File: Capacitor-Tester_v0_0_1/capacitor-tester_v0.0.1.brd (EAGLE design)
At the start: 100 x 80 mm, 6 parts, among them U1 AD5933, Y1 LFSPXO018034

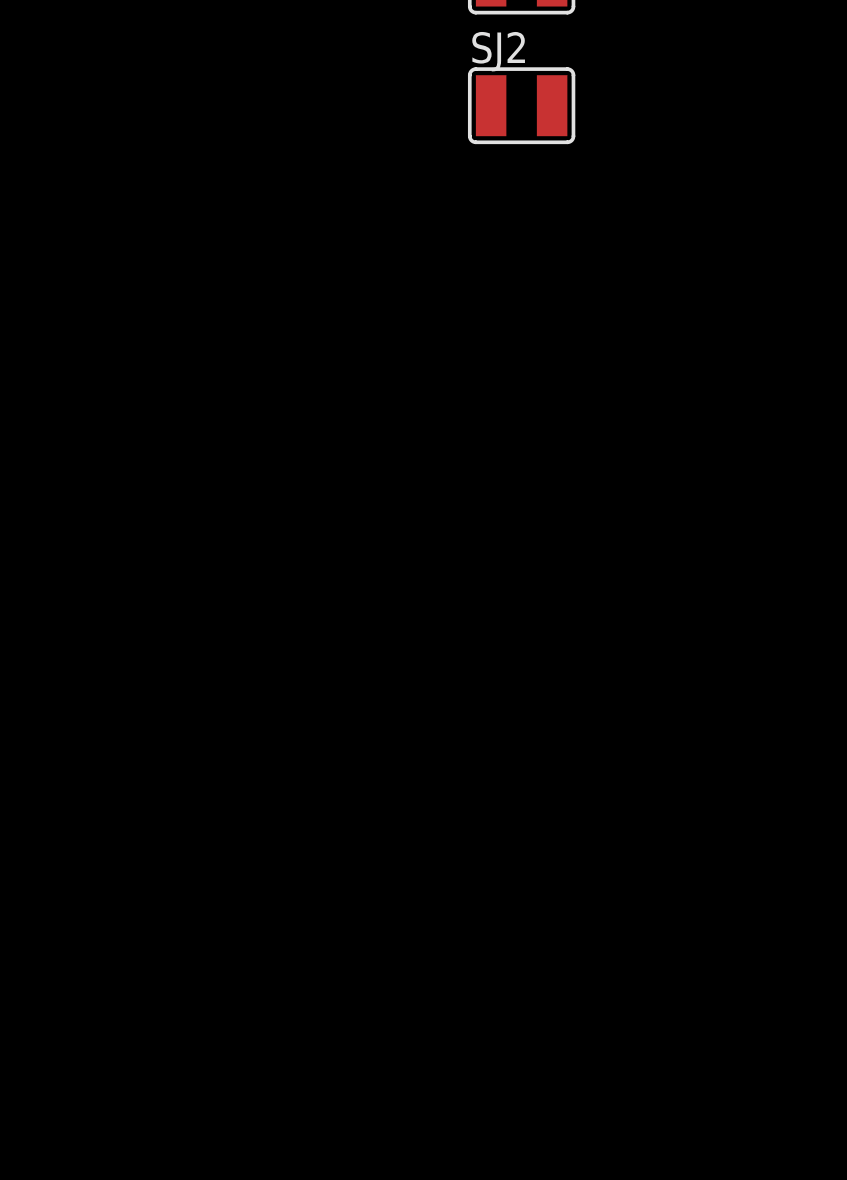
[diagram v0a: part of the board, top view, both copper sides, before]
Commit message: v0.0.1 - Finished the first stage of AD5933 opamp and added usb c connector for the power supply
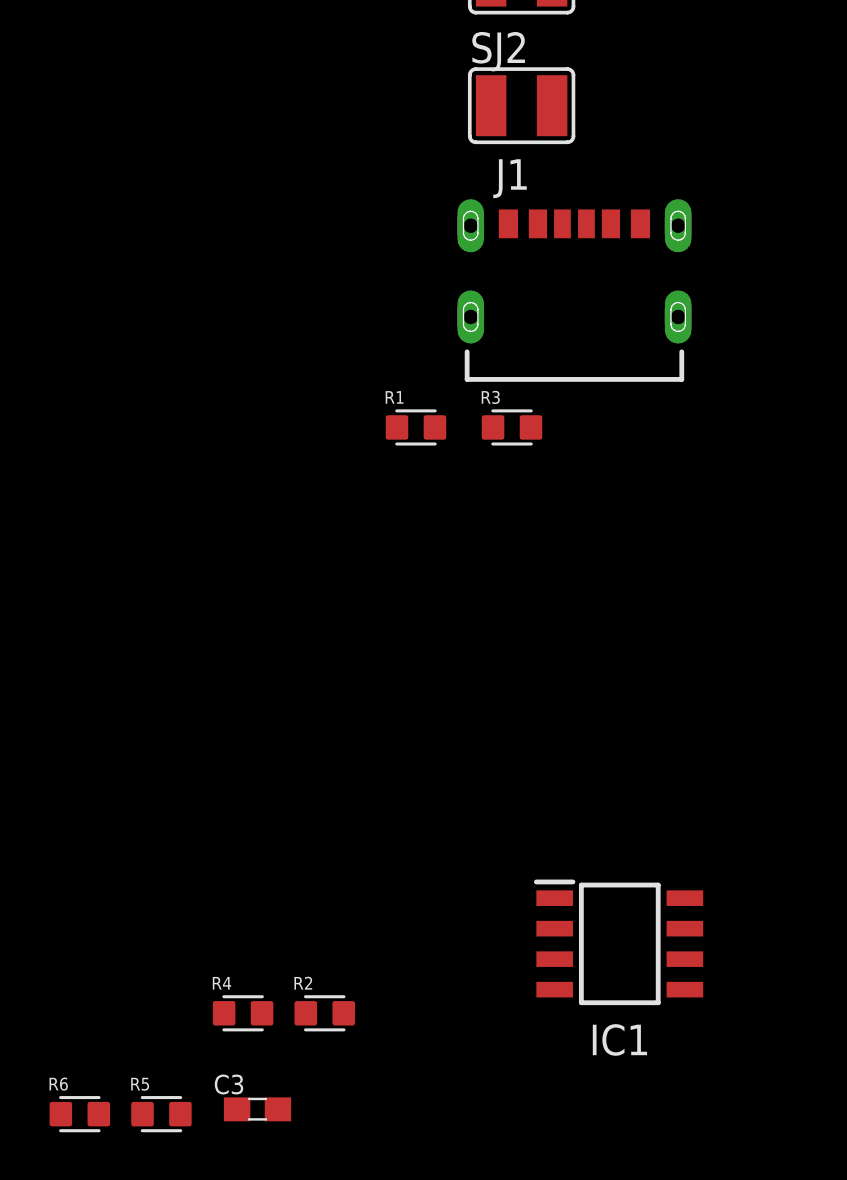
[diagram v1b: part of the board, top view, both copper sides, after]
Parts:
- added C3: 1u, custom_library:C0603
- added IC1: AD8531ARZ, AD8531ARZ:SOIC127P600X175-8N
- added J1: USB4125-GF-A-0190_REVA2, USB-C-6Pin:GCT_USB4125-GF-A-0190_REVA2
- added R1, R3: DNP4k7-1%, custom_library:R0603
- added R2, R5, R6: 20k-1%, custom_library:R0603
- added R4: 4k-1%, custom_library:R0603
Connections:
- new net N$1: IC1.2, R2.1, R4.1
- new net N$4: C3.1, IC1.3, R5.2, R6.1
- new net OPAMP_OUT: IC1.6, R4.2
- new net RFB: U1.4
- new net VIN: U1.5
- new net VOUT: R2.2, U1.6
- net +5V: now also IC1.7, J1.A9, J1.B9, R1.2, R3.2, R5.1
- net GND: now also C3.2, IC1.4, J1.A12, J1.B12, J1.S1, J1.S2, J1.S3, J1.S4, R6.2
- net SCL: now also R1.1
- net SDA: now also R3.1
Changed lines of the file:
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@@
 <attribute name="VALUE" x="-5.8" y="-73.4" size="0.02" layer="27"/>
+</element>
+<element name="J1" library="USB-C-6Pin" package="GCT_USB4125-GF-A-0190_REVA2" value="USB4125-GF-A-0190_REVA2" x="-4.6" y="-81.4" smashed="yes">
+<attribute name="AVAILABILITY" value="In Stock" x="-4.6" y="-81.4" size="1.778" layer="27" display="off"/>
+<attribute name="CHECK_PRICES" value="https://www.snapeda.com/parts/USB4125-GF-A-0190/Global+Connector+Technology/view-part/?ref=eda" x="-4.6" y="-81.4" size="1.778" layer="27" display="off"/>
+<attribute name="DESCRIPTION" value="                                                      USB-C (USB TYPE-C) USB 2.0 Receptacle Connector 24 (6+18 Dummy) Position Surface Mount, Right Angle; Through Hole                                              " x="-4.6" y="-81.4" size="1.778" layer="27" display="off"/>
+<attribute name="MF" value="Global Connector Technology" x="-4.6" y="-81.4" size="1.778" layer="27" display="off"/>
+<attribute name="MP" value="USB4125-GF-A-0190" x="-4.6" y="-81.4" size="1.778" layer="27" display="off"/>
+<attribute name="NAME" x="-7.9" y="-76.9" size="1.27" layer="25"/>
+<attribute name="PACKAGE" value="None" x="-4.6" y="-81.4" size="1.778" layer="27" display="off"/>
+<attribute name="PRICE" value="None" x="-4.6" y="-81.4" size="1.778" layer="27" display="off"/>
+<attribute name="SNAPEDA_LINK" value="https://www.snapeda.com/parts/USB4125-GF-A-0190/Global+Connector+Technology/view-part/?ref=snap" x="-4.6" y="-81.4" size="1.778" layer="27" display="off"/>
+</element>
+<element name="R3" library="custom_library" package="R0603" value="DNP4k7-1%" x="-7.2" y="-86.8" smashed="yes">
+<attribute name="NAME" x="-8.52476875" y="-85.813721875" size="0.52744375" layer="25"/>
+<attribute name="VALUE" x="-8.919259375" y="-88.32958125" size="0.525771875" layer="27"/>
+</element>
+<element name="R1" library="custom_library" package="R0603" value="DNP4k7-1%" x="-11.2" y="-86.8" smashed="yes">
+<attribute name="NAME" x="-12.52476875" y="-85.813721875" size="0.52744375" layer="25"/>
+<attribute name="VALUE" x="-12.919259375" y="-88.32958125" size="0.525771875" layer="27"/>
+</element>
+<element name="IC1" library="AD8531ARZ" package="SOIC127P600X175-8N" value="AD8531ARZ" x="-2.712" y="-108.31" smashed="yes">
+<attribute name="DESCRIPTION" value="250 mA Output, Low Cost, Single-Supply Amplifier" x="-2.712" y="-108.31" size="1.778" layer="27" display="off"/>
+<attribute name="HEIGHT" value="1.75mm" x="-2.712" y="-108.31" size="1.778" layer="27" display="off"/>
+<attribute name="MANUFACTURER_NAME" value="Analog Devices" x="-2.712" y="-108.31" size="1.778" layer="27" display="off"/>
+<attribute name="MANUFACTURER_PART_NUMBER" value="AD8531ARZ" x="-2.712" y="-108.31" size="1.778" layer="27" display="off"/>
+<attribute name="MOUSER_PART_NUMBER" value="584-AD8531ARZ" x="-2.712" y="-108.31" size="1.778" layer="27" display="off"/>
+<attribute name="MOUSER_PRICE-STOCK" value="https://www.mouser.co.uk/ProductDetail/Analog-Devices/AD8531ARZ?qs=%2FtpEQrCGXCxqCqynf0JWOw%3D%3D" x="-2.712" y="-108.31" size="1.778" layer="27" display="off"/>
+<attribute name="NAME" x="-2.712" y="-112.31" size="1.27" layer="25" align="center"/>
+<attribute name="VALUE" x="-2.712" y="-108.31" size="1.27" layer="27" align="center"/>
+</element>
+<element name="R2" library="custom_library" package="R0603" value="20k-1%" x="-15" y="-111.2" smashed="yes">
+<attribute name="NAME" x="-16.32476875" y="-110.213721875" size="0.52744375" layer="25"/>
+<attribute name="VALUE" x="-16.719259375" y="-112.72958125" size="0.525771875" layer="27"/>
+</element>
+<element name="R4" library="custom_library" package="R0603" value="4k-1%" x="-18.4" y="-111.2" smashed="yes">
+<attribute name="NAME" x="-19.72476875" y="-110.213721875" size="0.52744375" layer="25"/>
+<attribute name="VALUE" x="-20.119259375" y="-112.72958125" size="0.525771875" layer="27"/>
+</element>
+<element name="C3" library="custom_library" package="C0603" value="1u" x="-17.8" y="-115.2" smashed="yes">
+<attribute name="NAME" x="-19.635" y="-114.565" size="0.8" layer="25"/>
+<attribute name="VALUE" x="-18.435" y="-117.105" size="1.27" layer="27"/>
+</element>
+<element name="R5" library="custom_library" package="R0603" value="20k-1%" x="-21.8" y="-115.4" smashed="yes">
+<attribute name="NAME" x="-23.12476875" y="-114.413721875" size="0.52744375" layer="25"/>
+<attribute name="VALUE" x="-23.519259375" y="-116.92958125" size="0.525771875" layer="27"/>
+</element>
+<element name="R6" library="custom_library" package="R0603" value="20k-1%" x="-25.2" y="-115.4" smashed="yes">
+<attribute name="NAME" x="-26.52476875" y="-114.413721875" size="0.52744375" layer="25"/>
+<attribute name="VALUE" x="-26.919259375" y="-116.92958125" size="0.525771875" layer="27"/>
 </element>
 </elements>
@@
 <contactref element="C2" pad="2"/>
 <contactref element="Y1" pad="2"/>
+<contactref element="J1" pad="B12"/>
+<contactref element="J1" pad="A12"/>
+<contactref element="J1" pad="S1"/>
+<contactref element="J1" pad="S4"/>
+<contactref element="J1" pad="S2"/>
+<contactref element="J1" pad="S3"/>
+<contactref element="IC1" pad="4"/>
+<contactref element="C3" pad="2"/>
+<contactref element="R6" pad="2"/>
+<wire x1="-16.95" y1="-115.2" x2="-24.41" y2="-115.4" width="0" layer="19" extent="1-1"/>
+<wire x1="-5.424" y1="-110.215" x2="-16.95" y2="-115.2" width="0" layer="19" extent="1-1"/>
+<wire x1="-8.92" y1="-82.2" x2="-5.424" y2="-110.215" width="0" layer="19" extent="1-1"/>
+<wire x1="-8.92" y1="-78.4" x2="-8.92" y2="-82.2" width="0" layer="19" extent="1-1"/>
+<wire x1="-7.35" y1="-78.32" x2="-8.92" y2="-78.4" width="0" layer="19" extent="1-1"/>
+<wire x1="-1.85" y1="-78.32" x2="-7.35" y2="-78.32" width="0" layer="19" extent="1-1"/>
+<wire x1="-0.28" y1="-78.4" x2="-1.85" y2="-78.32" width="0" layer="19" extent="1-1"/>
+<wire x1="-0.28" y1="-82.2" x2="-0.28" y2="-78.4" width="0" layer="19" extent="1-1"/>
+<wire x1="0" y1="-59.8" x2="-0.28" y2="-78.4" width="0" layer="19" extent="1-1"/>
 <wire x1="-5.75" y1="-26.6" x2="0" y2="-59.8" width="0" layer="19" extent="1-1"/>
 <wire x1="-5.75" y1="-22.4" x2="-5.75" y2="-26.6" width="0" layer="19" extent="1-1"/>
@@
 <contactref element="Y1" pad="4"/>
 <contactref element="Y1" pad="1"/>
+<contactref element="J1" pad="B9"/>
+<contactref element="J1" pad="A9"/>
+<contactref element="R3" pad="2"/>
+<contactref element="R1" pad="2"/>
+<contactref element="IC1" pad="7"/>
+<contactref element="R5" pad="1"/>
+<wire x1="0" y1="-107.675" x2="-22.59" y2="-115.4" width="0" layer="19" extent="1-1"/>
+<wire x1="-6.41" y1="-86.8" x2="0" y2="-107.675" width="0" layer="19" extent="1-1"/>
+<wire x1="-10.41" y1="-86.8" x2="-6.41" y2="-86.8" width="0" layer="19" extent="1-1"/>
+<wire x1="-6.12" y1="-78.32" x2="-6.41" y2="-86.8" width="0" layer="19" extent="1-1"/>
+<wire x1="-3.08" y1="-78.32" x2="-6.12" y2="-78.32" width="0" layer="19" extent="1-1"/>
+<wire x1="-5.08" y1="-59.8" x2="-6.12" y2="-78.32" width="0" layer="19" extent="1-1"/>
 <wire x1="-5.08" y1="-55.6" x2="-5.08" y2="-59.8" width="0" layer="19" extent="1-1"/>
 <wire x1="-7.45" y1="-26.6" x2="-5.08" y2="-55.6" width="0" layer="19" extent="1-1"/>
@@
 <signal name="SCL">
 <contactref element="U1" pad="16"/>
+<contactref element="R1" pad="1"/>
+<wire x1="0" y1="-12.7" x2="-11.99" y2="-86.8" width="0" layer="19" extent="1-1"/>
 </signal>
 <signal name="SDA">
 <contactref element="U1" pad="15"/>
+<contactref element="R3" pad="1"/>
+<wire x1="0" y1="-13.35" x2="-7.99" y2="-86.8" width="0" layer="19" extent="1-1"/>
 </signal>
 <signal name="MCLK">
@@
 <contactref element="SJ2" pad="1"/>
 </signal>
+<signal name="RFB">
+<contactref element="U1" pad="4"/>
+</signal>
+<signal name="VIN">
+<contactref element="U1" pad="5"/>
+</signal>
+<signal name="VOUT">
+<contactref element="U1" pad="6"/>
+<contactref element="R2" pad="2"/>
+<wire x1="-7.01" y1="-15.95" x2="-14.21" y2="-111.2" width="0" layer="19" extent="1-1"/>
+</signal>
+<signal name="N$1">
+<contactref element="R2" pad="1"/>
+<contactref element="IC1" pad="2"/>
+<contactref element="R4" pad="1"/>
+<wire x1="-15.79" y1="-111.2" x2="-19.19" y2="-111.2" width="0" layer="19" extent="1-1"/>
+<wire x1="-5.424" y1="-107.675" x2="-15.79" y2="-111.2" width="0" layer="19" extent="1-1"/>
+</signal>
+<signal name="OPAMP_OUT">
+<contactref element="IC1" pad="6"/>
+<contactref element="R4" pad="2"/>
+<wire x1="0" y1="-108.945" x2="-17.61" y2="-111.2" width="0" layer="19" extent="1-1"/>
+</signal>
+<signal name="N$4">
+<contactref element="IC1" pad="3"/>
+<contactref element="C3" pad="1"/>
+<contactref element="R5" pad="2"/>
+<contactref element="R6" pad="1"/>
+<wire x1="-21.01" y1="-115.4" x2="-25.99" y2="-115.4" width="0" layer="19" extent="1-1"/>
+<wire x1="-18.65" y1="-115.2" x2="-21.01" y2="-115.4" width="0" layer="19" extent="1-1"/>
+<wire x1="-5.424" y1="-108.945" x2="-18.65" y2="-115.2" width="0" layer="19" extent="1-1"/>
+</signal>
 </signals>
